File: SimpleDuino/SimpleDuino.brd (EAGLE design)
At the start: 39.4 x 32.8 mm, 16 parts, among them J2 POWER_JACKPOWER_JACK_SMD, U1 V_REG_LD1117, U2 ATMEGA328P-PU, Y1 ABL-16.000MHZ-B4Y

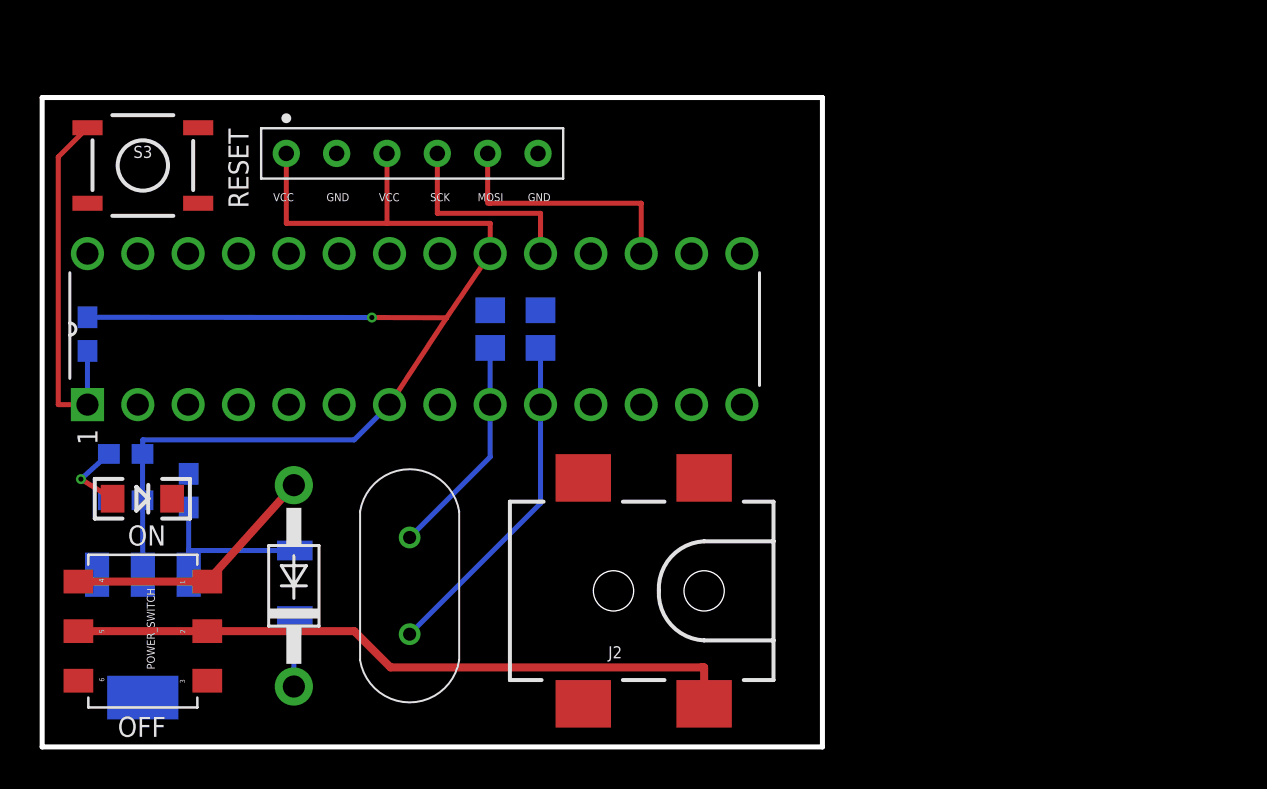
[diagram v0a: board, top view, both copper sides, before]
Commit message: Added additional headers and restructured pcb layout.
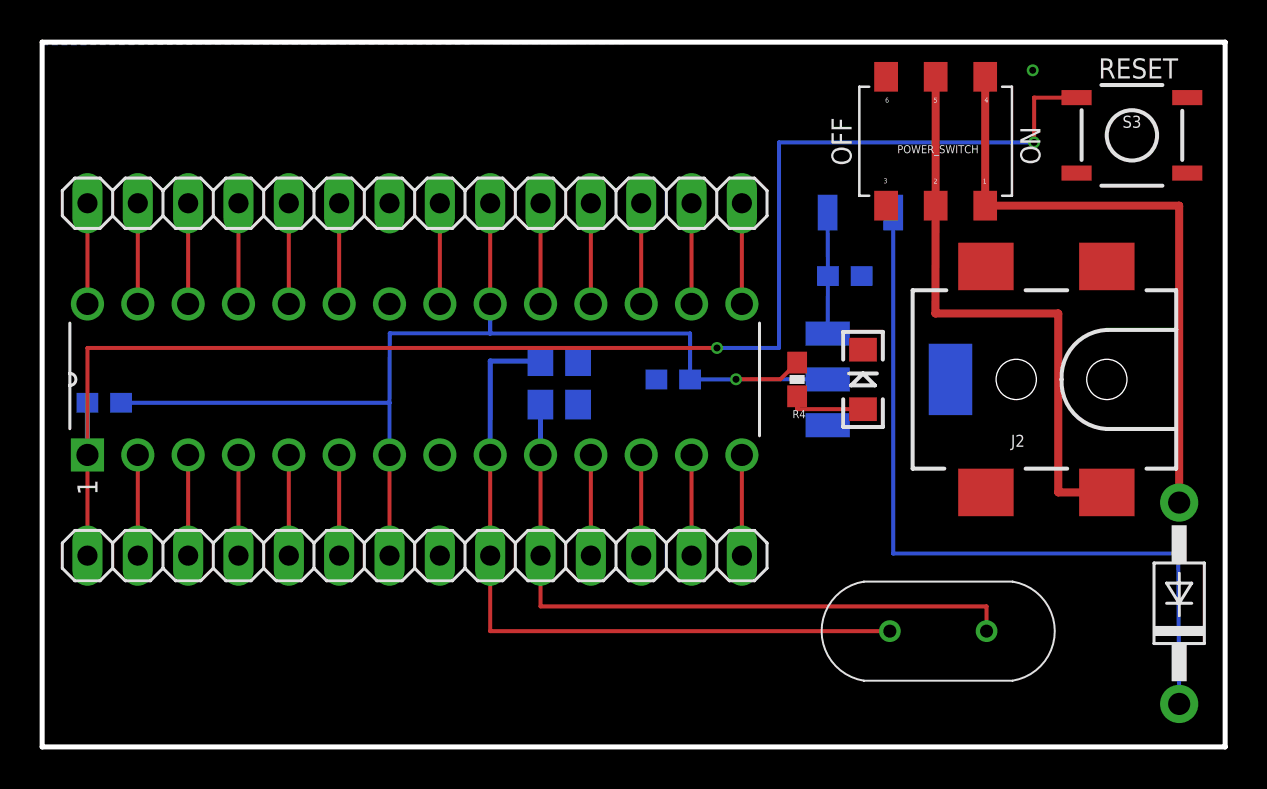
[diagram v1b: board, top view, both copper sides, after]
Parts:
- removed APA102_PINOUT: 929974-01-06-RK9, SamacSys_Parts:929974-01-06-RK
- added JP1, JP4: (no value), pinhead:1X14
- moved S3 49.9 mm to (55.0, 30.9)
- moved POWER_SWITCH 47.0 mm to (45.1, 30.6), turned to 180 degrees
- moved D1 44.7 mm to (57.4, 7.25)
- moved U1 39.8 mm to (42.7, 18.5), turned to 90 degrees
- moved LED2 36.9 mm to (41.4, 18.5), turned to 90 degrees
- moved C6 34.8 mm to (40.5, 23.8), turned to 180 degrees
- moved F1 34.1 mm to (41.3, 27.0), turned to 0 degrees
- moved R4 34.1 mm to (38.1, 18.5), flipped to the top, turned to 90 degrees
- moved C7 28.3 mm to (31.8, 18.5)
- moved Y1 26.8 mm to (45.2, 5.84), turned to 0 degrees
- moved J2 23.0 mm to (53.7, 18.5)
- moved C5 3.92 mm to (26.1, 17.3), turned to 180 degrees
- moved C4 3.84 mm to (26.1, 19.5), turned to 180 degrees
- moved R5 3.57 mm to (3.13, 17.4), turned to 0 degrees
- moved U2 2.54 mm to (35.3, 22.4)
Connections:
- removed net MOSI: APA102_PINOUT.5, U2.17
- removed net N$3: C4.1, U2.9, Y1.1
- removed net N$6: C5.1, U2.10, Y1.2
- removed net N$7: R5.2, S3.1, U2.1
- removed net SCK: APA102_PINOUT.4, U2.19
- new net 10_PB7: C5.1, JP1.10, U2.10, Y1.2
- new net 11_PD5: JP1.11, U2.11
- new net 12_PD6: JP1.12, U2.12
- new net 13_PD7: JP1.13, U2.13
- new net 14_PB0: JP1.14, U2.14
- new net 15_PB1: JP4.14, U2.15
- new net 16_PB2: JP4.13, U2.16
- new net 17_PB3: JP4.12, U2.17
- new net 18_PB4: JP4.11, U2.18
- new net 19_PB5: JP4.10, U2.19
- new net 1_PC6: JP1.1, R5.2, S3.1, U2.1
- new net 23_PC0: JP4.6, U2.23
- new net 24_PC1: JP4.5, U2.24
- new net 25_PC2: JP4.4, U2.25
- new net 26_PC3: JP4.3, U2.26
- new net 27_PC4: JP4.2, U2.27
- new net 28_PC5: JP4.1, U2.28
- new net 2_PD0: JP1.2, U2.2
- new net 3_PD1: JP1.3, U2.3
- new net 4_PD2: JP1.4, U2.4
- new net 5_PD3: JP1.5, U2.5
- new net 6_PD4: JP1.6, U2.6
- new net 9_PB6: C4.1, JP1.9, U2.9, Y1.1
- new net AREF: JP4.8, U2.21
- net GND: now also JP1.8, JP4.7; no longer APA102_PINOUT.2, APA102_PINOUT.6
- net VCC: now also JP1.7, JP4.9; no longer APA102_PINOUT.1, APA102_PINOUT.3
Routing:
- net 1_PC6: track 0.00 -> 75.6 mm, vias 0 -> 2
- net 9_PB6: track 0.00 -> 36.3 mm
- net N$1: track 4.07 -> 39.2 mm
- net 10_PB7: track 0.00 -> 33.9 mm
- net N$7: track 18.8 -> 0.00 mm
- net N$9: track 13.0 -> 31.3 mm
- net N$6: track 17.2 -> 0.00 mm
- net MOSI: track 12.9 -> 0.00 mm
- net N$3: track 11.2 -> 0.00 mm
- net SCK: track 10.3 -> 0.00 mm
- net VCC: track 66.1 -> 60.7 mm
- net 6_PD4: track 0.00 -> 5.08 mm
- net 5_PD3: track 0.00 -> 5.08 mm
- net 4_PD2: track 0.00 -> 5.08 mm
- net 3_PD1: track 0.00 -> 5.08 mm
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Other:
- board size 39.4 x 32.8 mm -> 59.7 x 35.6 mm
- board text removed: "GND"
- board text removed: "MOSI"
- board text removed: "SCK"
- board text removed: "VCC"
